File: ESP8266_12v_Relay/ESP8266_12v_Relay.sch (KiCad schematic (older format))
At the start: 41 parts, among them J1 691137710002, J2 691137710002, J3 691137710002, J4 691137710002, J5 Conn_01x06_Female, J6 691137710002, U1 ESP-WROOM-02D_M1102H3200PH3Q0_, U2 AP6502SP-13, U3 DMN2029USD-13, U4 DMN2029USD-13

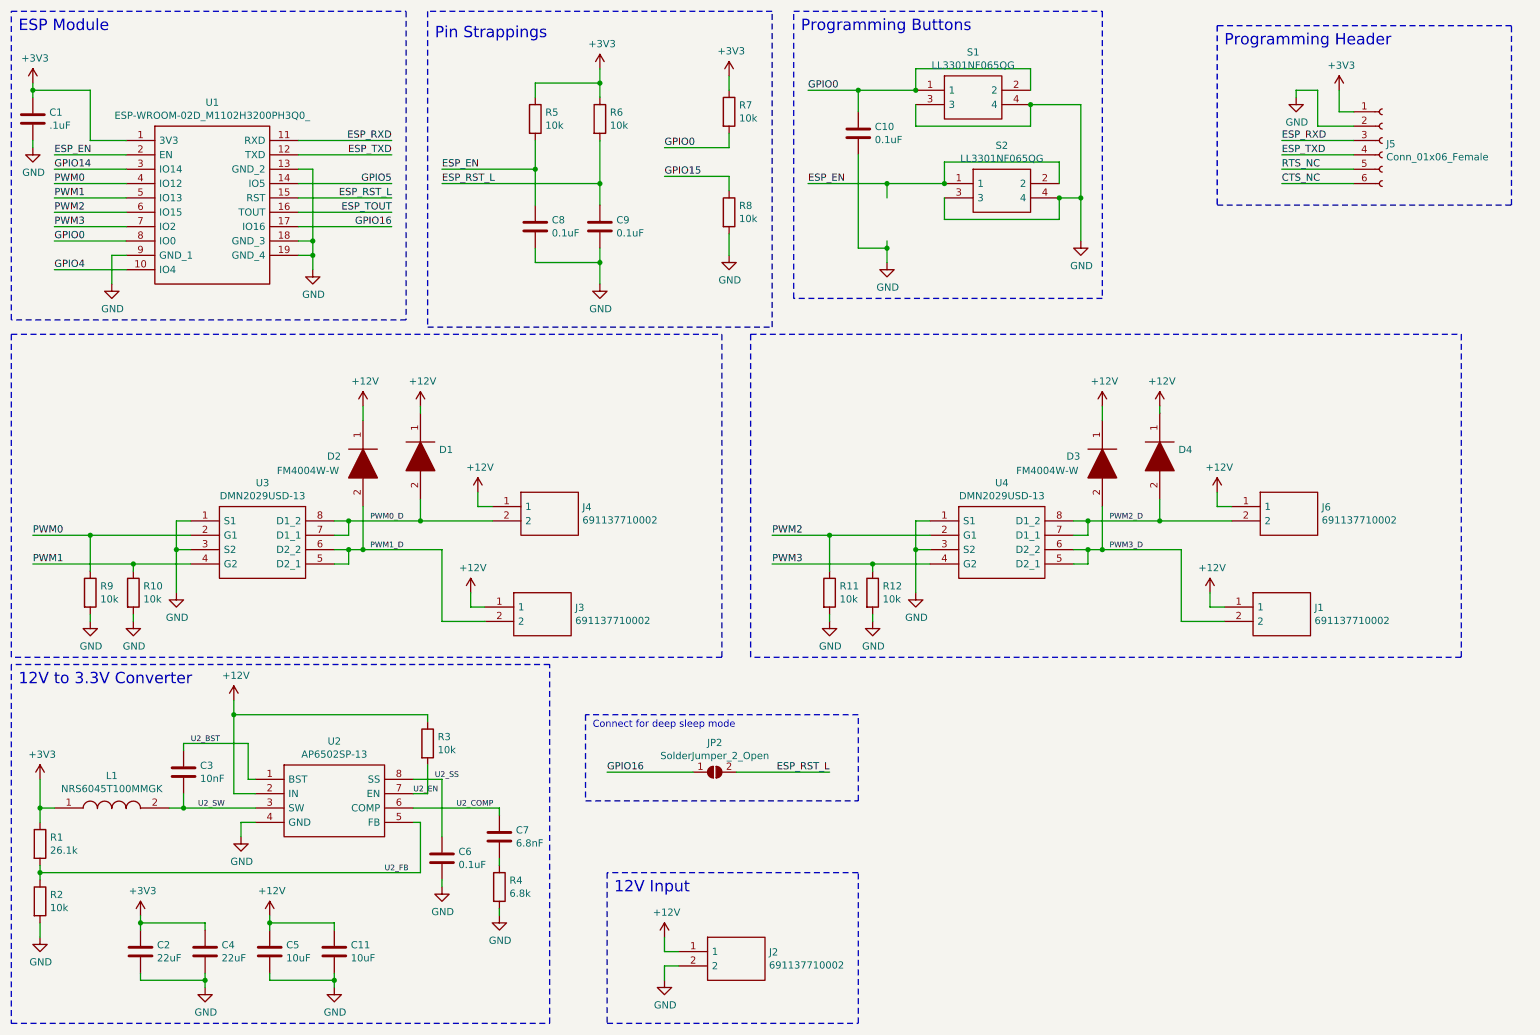
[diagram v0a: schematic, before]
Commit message: Started 12v relay design
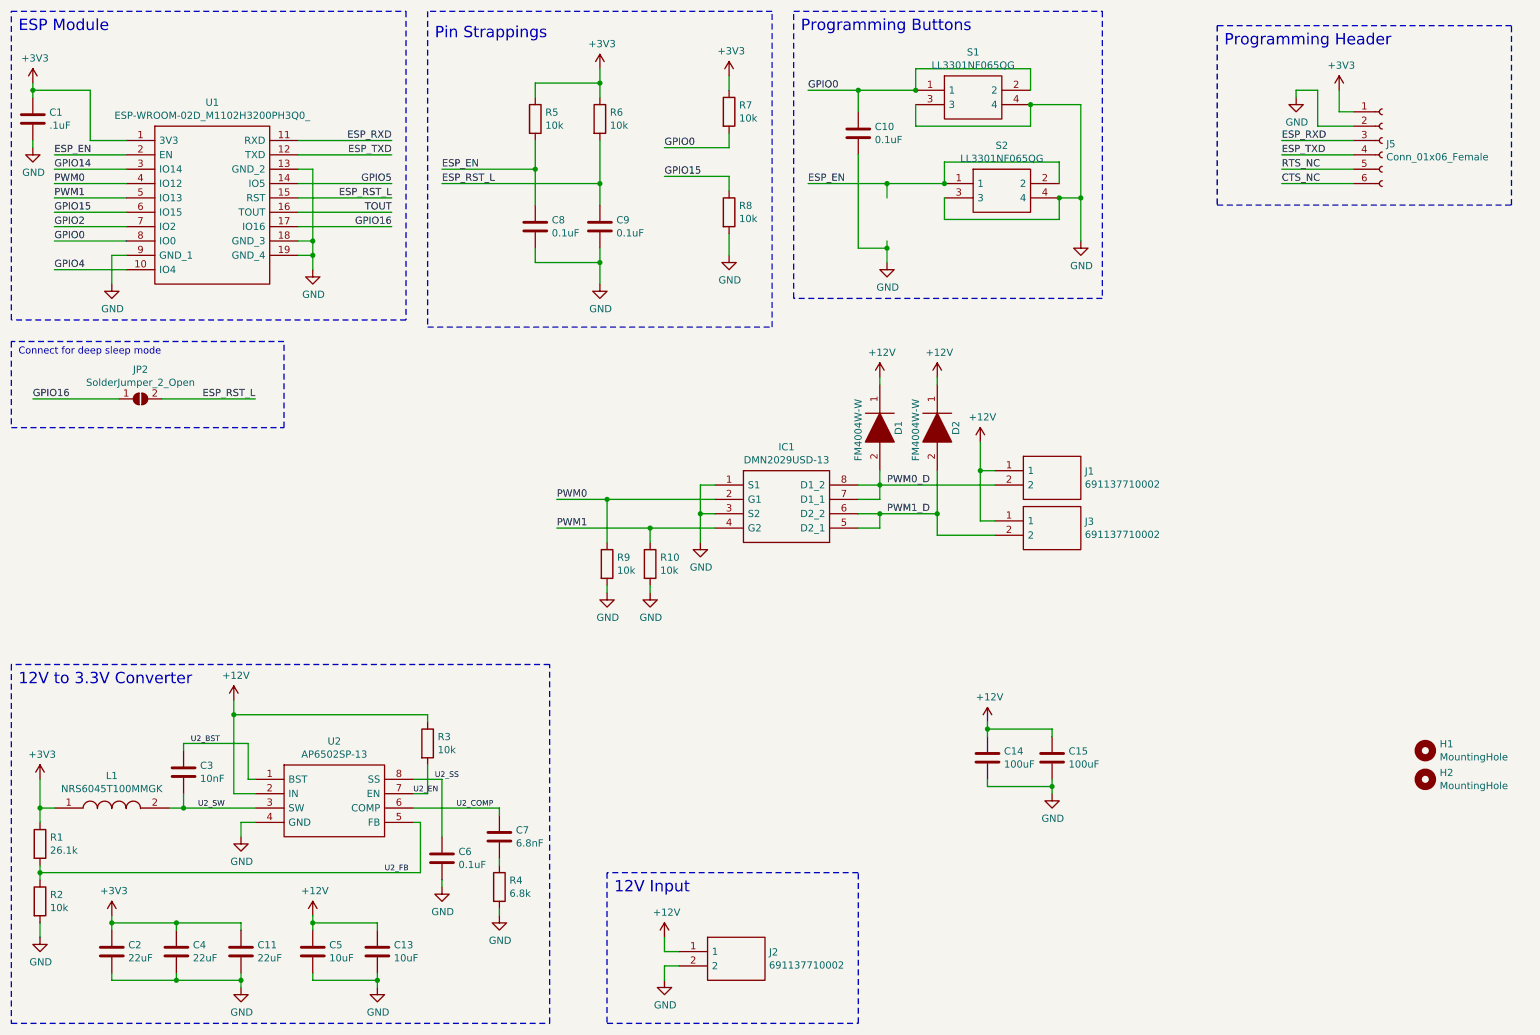
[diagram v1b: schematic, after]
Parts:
- removed D3, D4: FM4004W-W, SamacSys_Parts:DIOM5025X231N, symbol SamacSys_Parts:FM4004W-W
- removed J4, J6: 691137710002, SamacSys_Parts:SHDR2W70P0X500_1X2_1000X750X1160P, symbol SamacSys_Parts:691137710002
- removed R11, R12: 10k, Resistor_SMD:R_0805_2012Metric_Pad1.20x1.40mm_HandSolder, symbol Device:R
- removed U3, U4: DMN2029USD-13, SamacSys_Parts:SOIC127P600X175-8N, symbol SamacSys_Parts:DMN2029USD-13
- added C13: 10uF, Capacitor_SMD:C_0805_2012Metric_Pad1.18x1.45mm_HandSolder, symbol Device:C
- added C14, C15: 100uF, Capacitor_THT:CP_Radial_D6.3mm_P2.50mm, symbol Device:C
- added H1, H2: MountingHole, MountingHole:MountingHole_2.7mm_M2.5, symbol Mechanical:MountingHole
- added IC1: DMN2029USD-13, SamacSys_Parts:SOIC127P600X175-8N, symbol SamacSys_Parts:DMN2029USD-13
- C11: value 10uF -> 22uF
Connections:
- net PWM2 is gone; now on net GPIO15: U1.6 (IO15)
- net PWM3_D is gone; now on net PWM0_D: J1.2
- net +12V: now also C13.1, C14.1, C15.1; no longer C11.1
- net +3V3: now also C11.1
- net GND: now also C13.2, C14.2, C15.2, IC1.1 (S1), IC1.3 (S2)
- net PWM0: now also IC1.2 (G1)
- net PWM0_D: now also IC1.7 (D1_1), IC1.8 (D1_2)
- net PWM1: now also IC1.4 (G2)
- net PWM1_D: now also IC1.5 (D2_1), IC1.6 (D2_2)
- net ESP_TOUT renamed TOUT
- net PWM3 renamed GPIO2
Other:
- moved on the sheet: C2, C4, C5, JP2

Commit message: Finished 12v relay layout
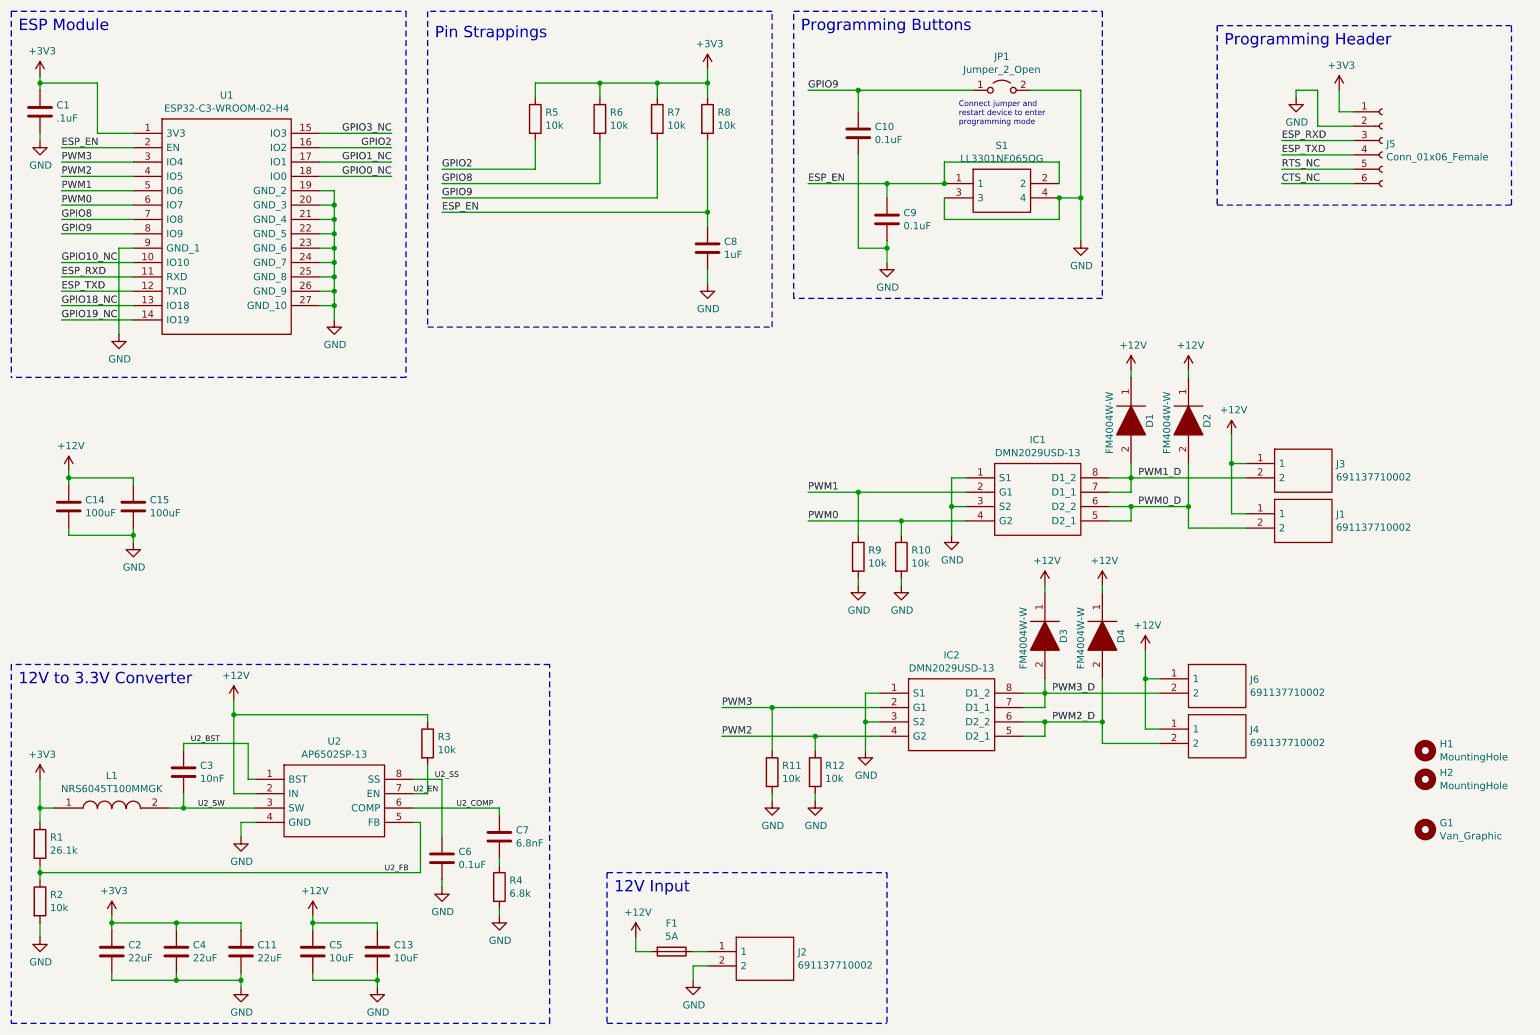
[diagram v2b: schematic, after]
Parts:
- removed JP2: SolderJumper_2_Open, Jumper:SolderJumper-2_P1.3mm_Open_RoundedPad1.0x1.5mm, symbol Jumper:SolderJumper_2_Open
- removed S2: LL3301NF065QG, SamacSys_Parts:LL3301NF065QG, symbol SamacSys_Parts:LL3301NF065QG
- removed U1: ESP-WROOM-02D_M1102H3200PH3Q0_, SamacSys_Parts:ESPWROOM02DM1102H3200PH3Q0, symbol SamacSys_Parts:ESP-WROOM-02D_M1102H3200PH3Q0_
- added D3, D4: FM4004W-W, SamacSys_Parts:DIOM5025X231N, symbol SamacSys_Parts:FM4004W-W
- added F1: 5A, Fuse:Fuse_1206_3216Metric_Pad1.42x1.75mm_HandSolder, symbol Device:Fuse
- added G1: Van_Graphic, SamacSys_Parts:van_pic, symbol Mechanical:MountingHole
- added IC2: DMN2029USD-13, SamacSys_Parts:SOIC127P600X175-8N, symbol SamacSys_Parts:DMN2029USD-13
- added J4, J6: 691137710002, SamacSys_Parts:SHDR2W70P0X500_1X2_1000X750X1160P, symbol SamacSys_Parts:691137710002
- added JP1: Jumper_2_Open, Connector_PinHeader_2.54mm:PinHeader_1x02_P2.54mm_Vertical, symbol Jumper:Jumper_2_Open
- added R11, R12: 10k, Resistor_SMD:R_0805_2012Metric_Pad1.20x1.40mm_HandSolder, symbol Device:R
- added U1: ESP32-C3-WROOM-02-H4, SamacSys_Parts:ESP32C3WROOM02H4, symbol SamacSys_Parts:ESP32-C3-WROOM-02-H4
- C8: value 0.1uF -> 1uF
- renumbered J3 to J1, J1 to J3
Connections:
- net GPIO15 is gone; now on net +3V3: R8.1
- net +12V: now also D3.1, D4.1, F1.2, J4.1, J6.1; no longer J2.1
- net +3V3: now also U1.1 (3V3)
- net ESP_EN: now also C9.1, R8.2, S1.1, S1.2, U1.2 (EN); no longer R5.2
- net ESP_RXD: now also U1.11 (RXD)
- net ESP_TXD: now also U1.12 (TXD)
- net GND: now also IC2.1 (S1), IC2.3 (S2), JP1.2 (B), R11.2, R12.2, U1.19 (GND_2), U1.20 (GND_3), U1.21 (GND_4), U1.22 (GND_5), U1.23 (GND_6), U1.24 (GND_7), U1.25 (GND_8), U1.26 (GND_9), U1.27 (GND_10), U1.9 (GND_1); no longer R8.2
- net GPIO2: now also R5.2, U1.16 (IO2)
- net PWM0: now also IC1.4 (G2), R10.1, U1.6 (IO7); no longer IC1.2 (G1), R9.1
- net PWM0_D: now also D2.2, IC1.5 (D2_1), IC1.6 (D2_2), J1.2; no longer D1.2, IC1.7 (D1_1), IC1.8 (D1_2), J3.2
- net PWM1: now also IC1.2 (G1), R9.1, U1.5 (IO6); no longer IC1.4 (G2), R10.1
- net PWM1_D: now also D1.2, IC1.7 (D1_1), IC1.8 (D1_2), J3.2; no longer D2.2, IC1.5 (D2_1), IC1.6 (D2_2), J1.2
- net ESP_RST_L renamed GPIO8
- net GPIO8: now also U1.7 (IO8); no longer C9.1
- net GPIO0 renamed GPIO9
- net GPIO9: now also JP1.1 (A), U1.8 (IO9); no longer S1.1, S1.2
- new net: F1.1, J2.1
- new net GPIO0_NC: U1.18 (IO0)
- new net GPIO10_NC: U1.10 (IO10)
- new net GPIO18_NC: U1.13 (IO18)
- new net GPIO19_NC: U1.14 (IO19)
- new net GPIO1_NC: U1.17 (IO1)
- new net GPIO3_NC: U1.15 (IO3)
- new net PWM2: IC2.4 (G2), R12.1, U1.4 (IO5)
- new net PWM2_D: D4.2, IC2.5 (D2_1), IC2.6 (D2_2), J4.2
- new net PWM3: IC2.2 (G1), R11.1, U1.3 (IO4)
- new net PWM3_D: D3.2, IC2.7 (D1_1), IC2.8 (D1_2), J6.2
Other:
- note added: "Connect jumper and\nrestart device to enter\nprogramming mode"
- note removed: "Connect for deep sleep mode"
- moved on the sheet: C1, C14, C15, C8, C9, D1, D2, IC1, J1, J2, J3, R10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

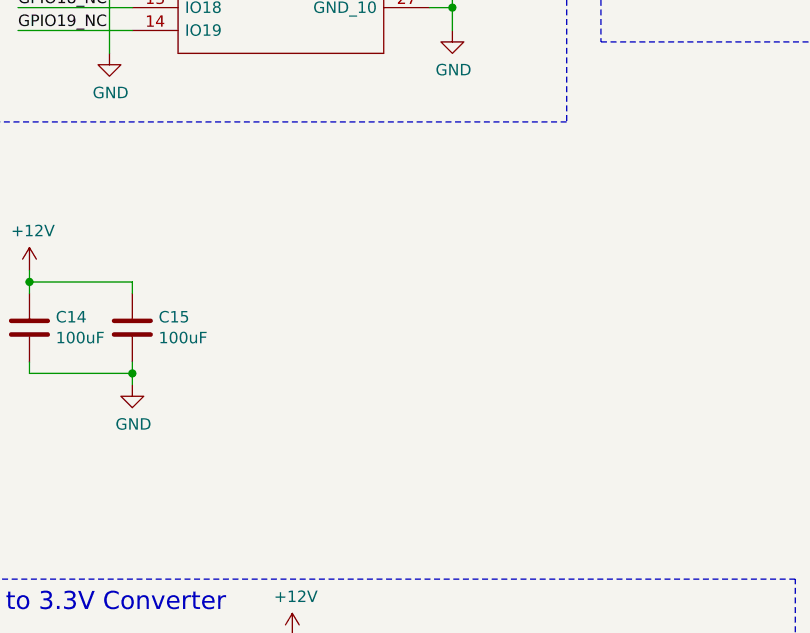
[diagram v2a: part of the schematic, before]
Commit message: Added LEDs to 12v relay
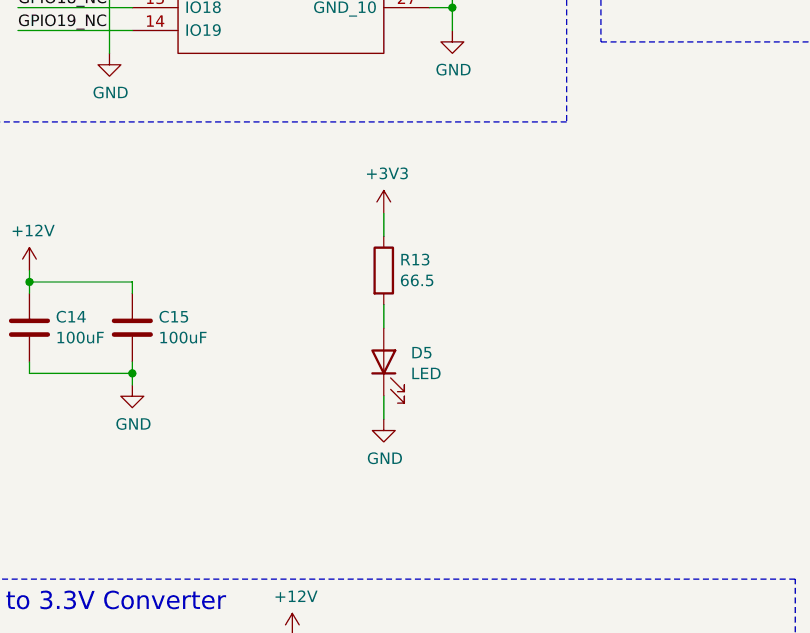
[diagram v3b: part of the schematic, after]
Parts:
- added D5: LED, LED_SMD:LED_0805_2012Metric_Pad1.15x1.40mm_HandSolder, symbol Device:LED
- added R13: 66.5, Resistor_SMD:R_0805_2012Metric_Pad1.20x1.40mm_HandSolder, symbol Device:R
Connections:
- net +3V3: now also R13.1
- net GND: now also D5.1 (K)
- new net: D5.2 (A), R13.2
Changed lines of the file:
@@
 	1    0    0    -1
 $EndComp
+$Comp
+L Device:LED D5
+U 1 1 61711833
+P 2550 4200
+F 0 "D5" V 2589 4082 50  0000 R CNN
+F 1 "LED" V 2498 4082 50  0000 R CNN
+F 2 "LED_SMD:LED_0805_2012Metric_Pad1.15x1.40mm_HandSolder" H 2550 4200 50  0001 C CNN
+F 3 "~" H 2550 4200 50  0001 C CNN
+	1    2550 4200
+	0    -1   -1   0
+$EndComp
+$Comp
+L Device:R R13
+U 1 1 61713B87
+P 2550 3800
+F 0 "R13" H 2620 3846 50  0000 L CNN
+F 1 "66.5" H 2620 3755 50  0000 L CNN
+F 2 "Resistor_SMD:R_0805_2012Metric_Pad1.20x1.40mm_HandSolder" V 2480 3800 50  0001 C CNN
+F 3 "~" H 2550 3800 50  0001 C CNN
+	1    2550 3800
+	1    0    0    -1
+$EndComp
+$Comp
+L power:+3V3 #PWR033
+U 1 1 61714614
+P 2550 3550
+F 0 "#PWR033" H 2550 3400 50  0001 C CNN
+F 1 "+3V3" H 2565 3723 50  0000 C CNN
+F 2 "" H 2550 3550 50  0001 C CNN
+F 3 "" H 2550 3550 50  0001 C CNN
+	1    2550 3550
+	1    0    0    -1
+$EndComp
+$Comp
+L power:GND #PWR036
+U 1 1 61714E83
+P 2550 4450
+F 0 "#PWR036" H 2550 4200 50  0001 C CNN
+F 1 "GND" H 2555 4277 50  0000 C CNN
+F 2 "" H 2550 4450 50  0001 C CNN
+F 3 "" H 2550 4450 50  0001 C CNN
+	1    2550 4450
+	1    0    0    -1
+$EndComp
+Wire Wire Line
+	2550 3550 2550 3650
+Wire Wire Line
+	2550 3950 2550 4050
+Wire Wire Line
+	2550 4350 2550 4450
 $EndSCHEMATC
